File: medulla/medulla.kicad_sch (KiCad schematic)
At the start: 0 parts

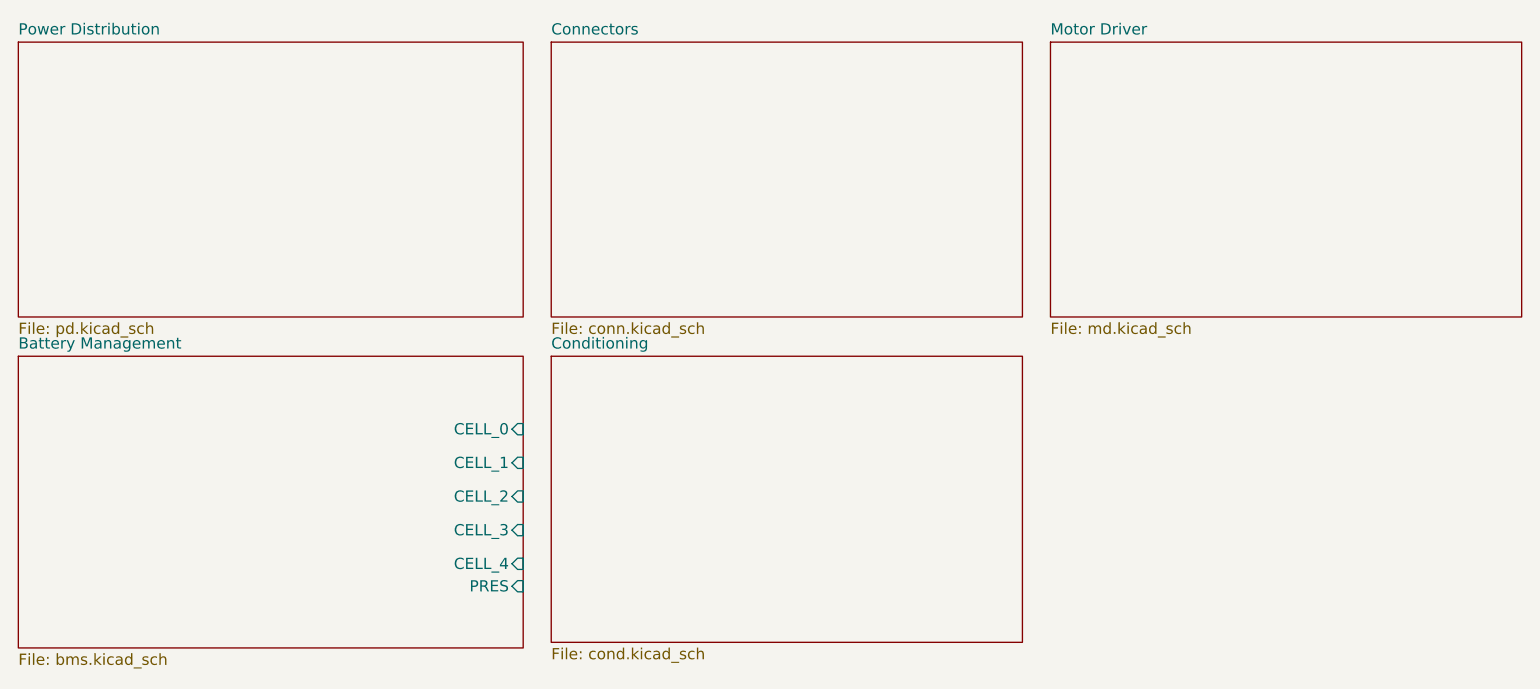
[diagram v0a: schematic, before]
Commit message: 0.1.3-alpha: H-Bridge Completion & I2C Sensor integration
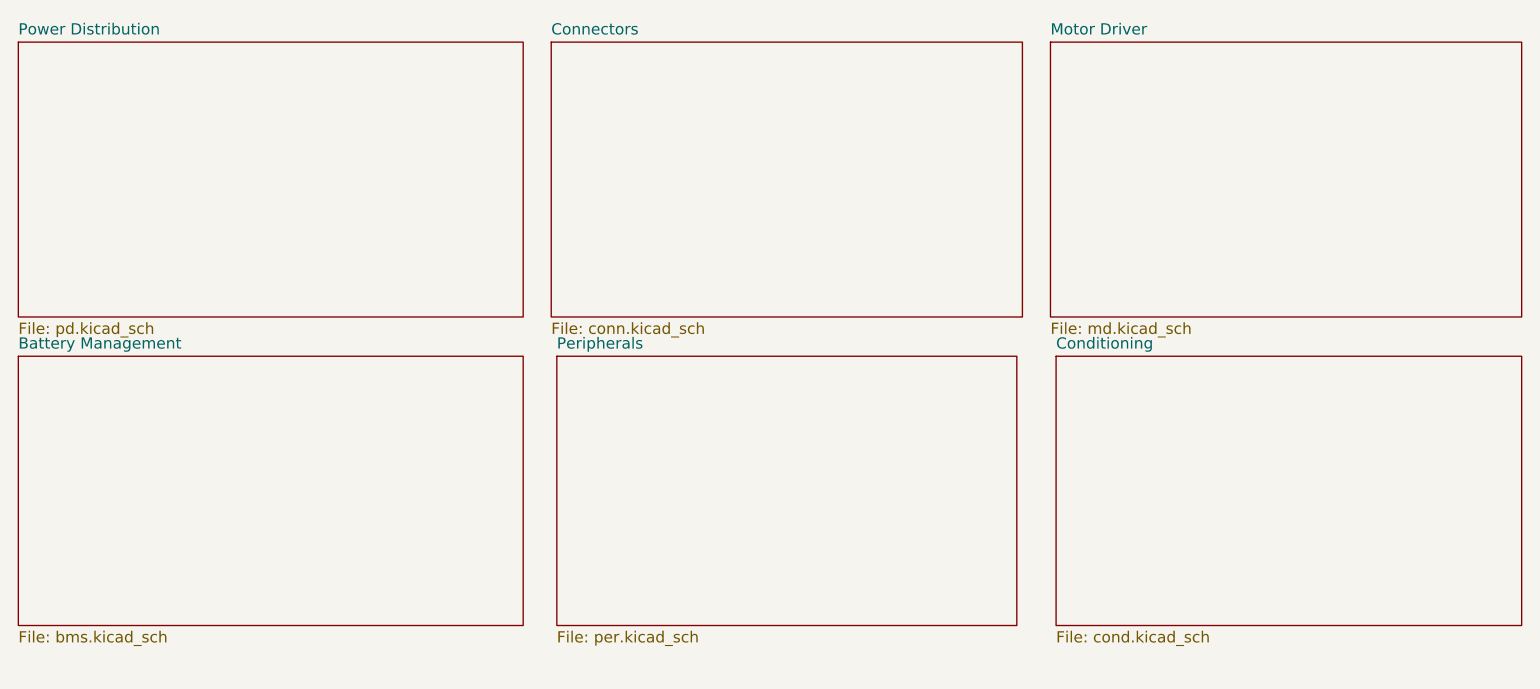
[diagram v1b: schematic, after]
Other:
- added sheet Peripherals (per.kicad_sch)
- sheet Battery Management ports: added none; removed CELL_0, CELL_1, CELL_2, CELL_3, CELL_4, PRES
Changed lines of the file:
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@@
 		)
 		(instances
-			(project "mitochondria"
+			(project "medulla"
 				(path "/d5881702-98ec-4aea-8d9c-3c163ba85aa3"
 					(page "3")
@@
 	(sheet
 		(at 17.78 52.07)
-		(size 57.15 33.02)
+		(size 57.15 30.48)
 		(exclude_from_sim no)
 		(in_bom yes)
@@
 		)
 		(property "Sheetfile" "bms.kicad_sch"
-			(at 17.78 85.6746 0)
-			(effects
-				(font
-					(size 1.27 1.27)
-				)
-				(justify left top)
-			)
-		)
-		(pin "CELL_0" input
-			(at 74.93 60.325 0)
-			(effects
-				(font
-					(size 1.27 1.27)
-				)
-				(justify right)
-			)
-		)
-		(pin "CELL_1" input
-			(at 74.93 64.135 0)
-			(effects
-				(font
-					(size 1.27 1.27)
-				)
-				(justify right)
-			)
-		)
-		(pin "CELL_2" input
-			(at 74.93 67.945 0)
-			(effects
-				(font
-					(size 1.27 1.27)
-				)
-				(justify right)
-			)
-		)
-		(pin "CELL_3" input
-			(at 74.93 71.755 0)
-			(effects
-				(font
-					(size 1.27 1.27)
-				)
-				(justify right)
-			)
-		)
-		(pin "CELL_4" input
-			(at 74.93 75.565 0)
-			(effects
-				(font
-					(size 1.27 1.27)
-				)
-				(justify right)
-			)
-		)
-		(pin "PRES" input
-			(at 74.93 78.105 0)
-			(effects
-				(font
-					(size 1.27 1.27)
-				)
-				(justify right)
-			)
-		)
-		(instances
-			(project "mitochondria"
+			(at 17.78 83.1346 0)
+			(effects
+				(font
+					(size 1.27 1.27)
+				)
+				(justify left top)
+			)
+		)
+		(instances
+			(project "medulla"
 				(path "/d5881702-98ec-4aea-8d9c-3c163ba85aa3"
 					(page "4")
@@
 	)
 	(sheet
-		(at 78.105 52.07)
-		(size 53.34 32.385)
+		(at 135.255 52.07)
+		(size 52.705 30.48)
 		(exclude_from_sim no)
 		(in_bom yes)
@@
 		)
 		(property "Sheetname" "Conditioning"
-			(at 78.105 51.3584 0)
+			(at 135.255 51.3584 0)
 			(effects
 				(font
@@
 		)
 		(property "Sheetfile" "cond.kicad_sch"
-			(at 78.105 85.0396 0)
-			(effects
-				(font
-					(size 1.27 1.27)
-				)
-				(justify left top)
-			)
-		)
-		(instances
-			(project "mitochondria"
+			(at 135.255 83.1346 0)
+			(effects
+				(font
+					(size 1.27 1.27)
+				)
+				(justify left top)
+			)
+		)
+		(instances
+			(project "medulla"
 				(path "/d5881702-98ec-4aea-8d9c-3c163ba85aa3"
 					(page "5")
@@
 		)
 		(instances
-			(project "mitochondria"
+			(project "medulla"
 				(path "/d5881702-98ec-4aea-8d9c-3c163ba85aa3"
 					(page "6")
+				)
+			)
+		)
+	)
+	(sheet
+		(at 78.74 52.07)
+		(size 52.07 30.48)
+		(exclude_from_sim no)
+		(in_bom yes)
+		(on_board yes)
+		(dnp no)
+		(fields_autoplaced yes)
+		(stroke
+			(width 0.1524)
+			(type solid)
+		)
+		(fill
+			(color 0 0 0 0.0000)
+		)
+		(property "Sheetname" "Peripherals"
+			(at 78.74 51.3584 0)
+			(effects
+				(font
+					(size 1.27 1.27)
+				)
+				(justify left bottom)
+			)
+		)
+		(property "Sheetfile" "per.kicad_sch"
+			(at 78.74 83.1346 0)
+			(effects
+				(font
+					(size 1.27 1.27)
+				)
+				(justify left top)
+			)
+		)
+		(property "Field2" ""
+			(at 78.74 52.07 0)
+			(effects
+				(font
+					(size 1.27 1.27)
+				)
+				(hide yes)
+			)
+		)
+		(instances
+			(project "medulla"
+				(path "/d5881702-98ec-4aea-8d9c-3c163ba85aa3"
+					(page "7")
 				)
 			)
@@
 		)
 		(instances
-			(project "mitochondria"
+			(project "medulla"
 				(path "/d5881702-98ec-4aea-8d9c-3c163ba85aa3"
 					(page "2")
